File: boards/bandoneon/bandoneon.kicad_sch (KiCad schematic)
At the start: 3 parts, among them J1 Conn_01x10_Pin, J2 Conn_01x10_Pin

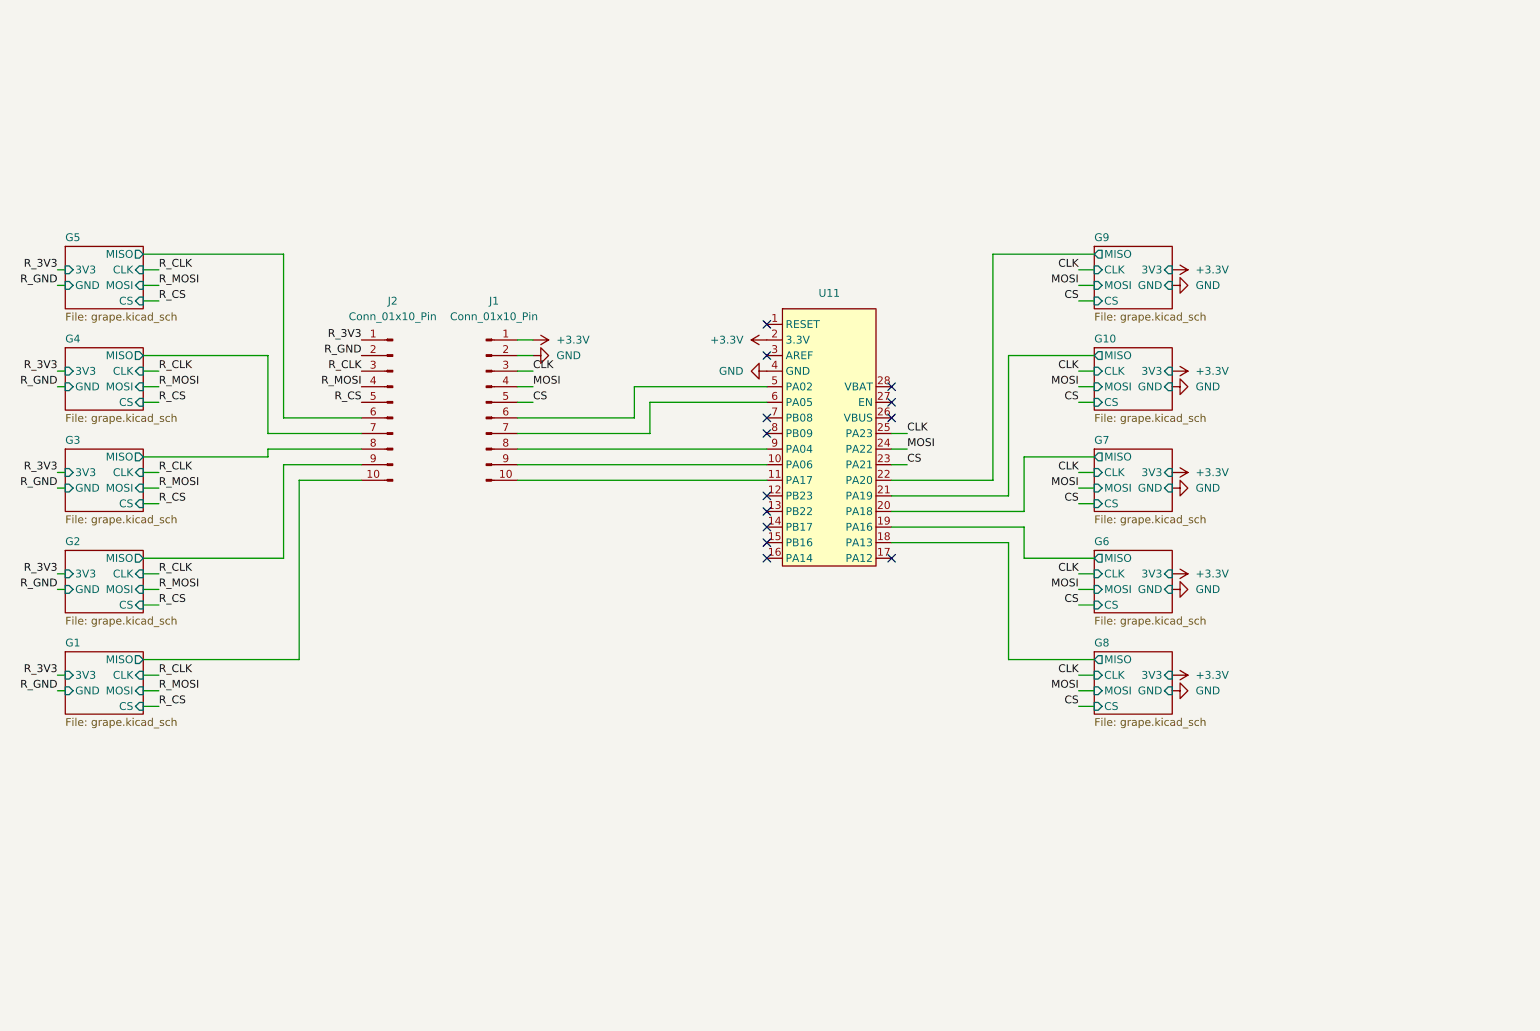
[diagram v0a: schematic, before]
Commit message: Use keyboard layout and set images DPI
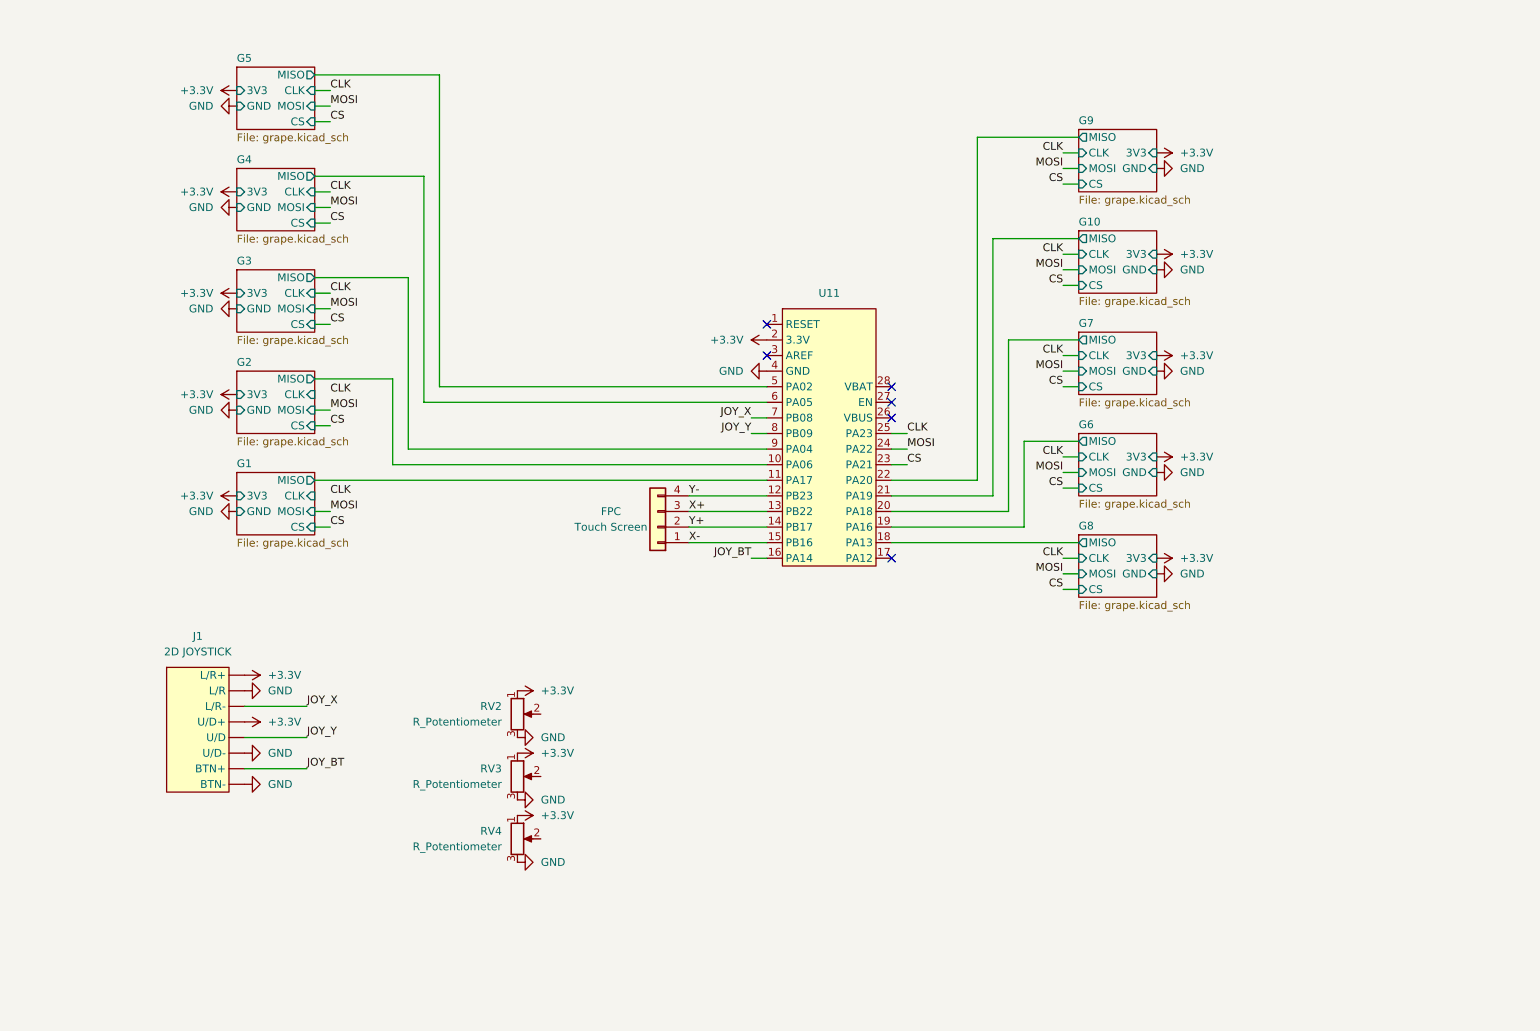
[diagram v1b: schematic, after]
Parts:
- removed J1, J2: Conn_01x10_Pin, Connector_PinHeader_1.27mm:PinHeader_1x10_P1.27mm_Vertical, symbol Connector:Conn_01x10_Pin
- added FPC: Touch Screen, Connector_FFC-FPC:TE_84952-4_1x04-1MP_P1.0mm_Horizontal, symbol Connector_Generic:Conn_01x04
- added J1: 2D JOYSTICK, symbol Library:2-Axis_Joystick
- added RV2, RV3, RV4: R_Potentiometer, symbol Device:R_Potentiometer
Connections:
- net +3.3V: now also J1. (U/D-), RV2.1, RV3.1, RV4.1
- net G1/MISO: now also U11.11 (PA17)
- net G2/MISO: now also U11.10 (PA06)
- net G3/MISO: now also U11.9 (PA04)
- net G4/MISO: now also U11.6 (PA05)
- net G5/MISO: now also U11.5 (PA02)
- net GND: now also J1. (U/D-), RV2.3, RV3.3, RV4.3
- net Y-: now reaches U11.12 (PB23)
- net Y-: now also FPC.4 (Pin_4)
- net X+: now reaches U11.13 (PB22)
- net X+: now also FPC.3 (Pin_3)
- net Y+: now reaches U11.14 (PB17)
- net Y+: now also FPC.2 (Pin_2)
- net X-: now reaches U11.15 (PB16)
- net X-: now also FPC.1 (Pin_1)
- net JOY_BT: now reaches U11.16 (PA14)
- net JOY_BT: now also J1. (U/D-)
- net JOY_X: now reaches U11.7 (PB08)
- net JOY_X: now also J1. (U/D-)
- net JOY_Y: now reaches U11.8 (PB09)
- net JOY_Y: now also J1. (U/D-)
- no-connect marks 13 -> 6

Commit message: Schamtic complete
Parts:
- removed RV3, RV4: R_Potentiometer, symbol Device:R_Potentiometer
- added J2: JST XH-3A, Connector_JST:JST_XH_B3B-XH-A_1x03_P2.50mm_Vertical, symbol Connector:Conn_01x03_Socket
- added J3: JST XH-3A, symbol Connector:Conn_01x03_Socket
- J1: footprint (none) -> Library:Adafruit (512) Analog 2-axis Thumb Joystick with Select Button
- renumbered FPC to FPC_1mm1
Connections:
- net G8/MISO is gone; now on net G1/MISO: U11.18 ((22)PA13)
- net +3.3V: now also J1.2 (X+), J1.5 (Y+), J2.3 (Pin_3); no longer J1. (U/D-), RV2.1
- net G1/MISO: no longer U11.11 (PA17)
- net G2/MISO: now also U11.16 (PA14(4)); no longer U11.10 (PA06)
- net G3/MISO: now also U11.11 (PA17(25)); no longer U11.9 (PA04)
- net G4/MISO: now also U11.10 (PA06(19/A5)); no longer U11.6 (PA05)
- net G5/MISO: now also U11.17 ((21)PA12); no longer U11.5 (PA02)
- net GND: now also J1.0 (X-), J1.3 (Y-), J1.6 (BTN-), J2.1 (Pin_1); no longer J1. (U/D-), RV2.3
- net JOY_BT: now also J1.7 (BTN+), U11.14 (PB17(0)); no longer J1. (U/D-), U11.16 (PA14)
- net JOY_X: now also J1.1 (X), U11.5 (PA02(14/A0)); no longer J1. (U/D-), U11.7 (PB08)
- net JOY_Y: now also J1.4 (Y), U11.6 (PA05(15/A1)); no longer J1. (U/D-), U11.8 (PB09)
- net at RV2.2: now also J3.2 (Pin_2)
- net X+ renamed SCR_X+
- net SCR_X+: now also U11.12 (PB23(24)); no longer U11.13 (PB22)
- net X-: no longer names the net of U11.15 (PB16(1))
- net X-: no longer FPC_1mm1.1 (Pin_1)
- net Y+ renamed SCR_Y+
- net SCR_Y+: now also U11.8 (PB09(17/A3)); no longer U11.14 (PB17)
- net Y- renamed SCR_Y-
- net SCR_Y-: now also U11.13 (PB22(23)); no longer U11.12 (PB23)
- new net: J3.3 (Pin_3), RV2.1
- new net: J3.1 (Pin_1), RV2.3
- new net POT: J2.2 (Pin_2), U11.9 (PA04(18/A4))
- new net SCR_X-: FPC_1mm1.1 (Pin_1), U11.7 (PB08(16/A2))
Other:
- removed sheet G8
- note added: "Analog reading out of Y+ and X-"
- moved on the sheet: FPC_1mm1, RV2, U11

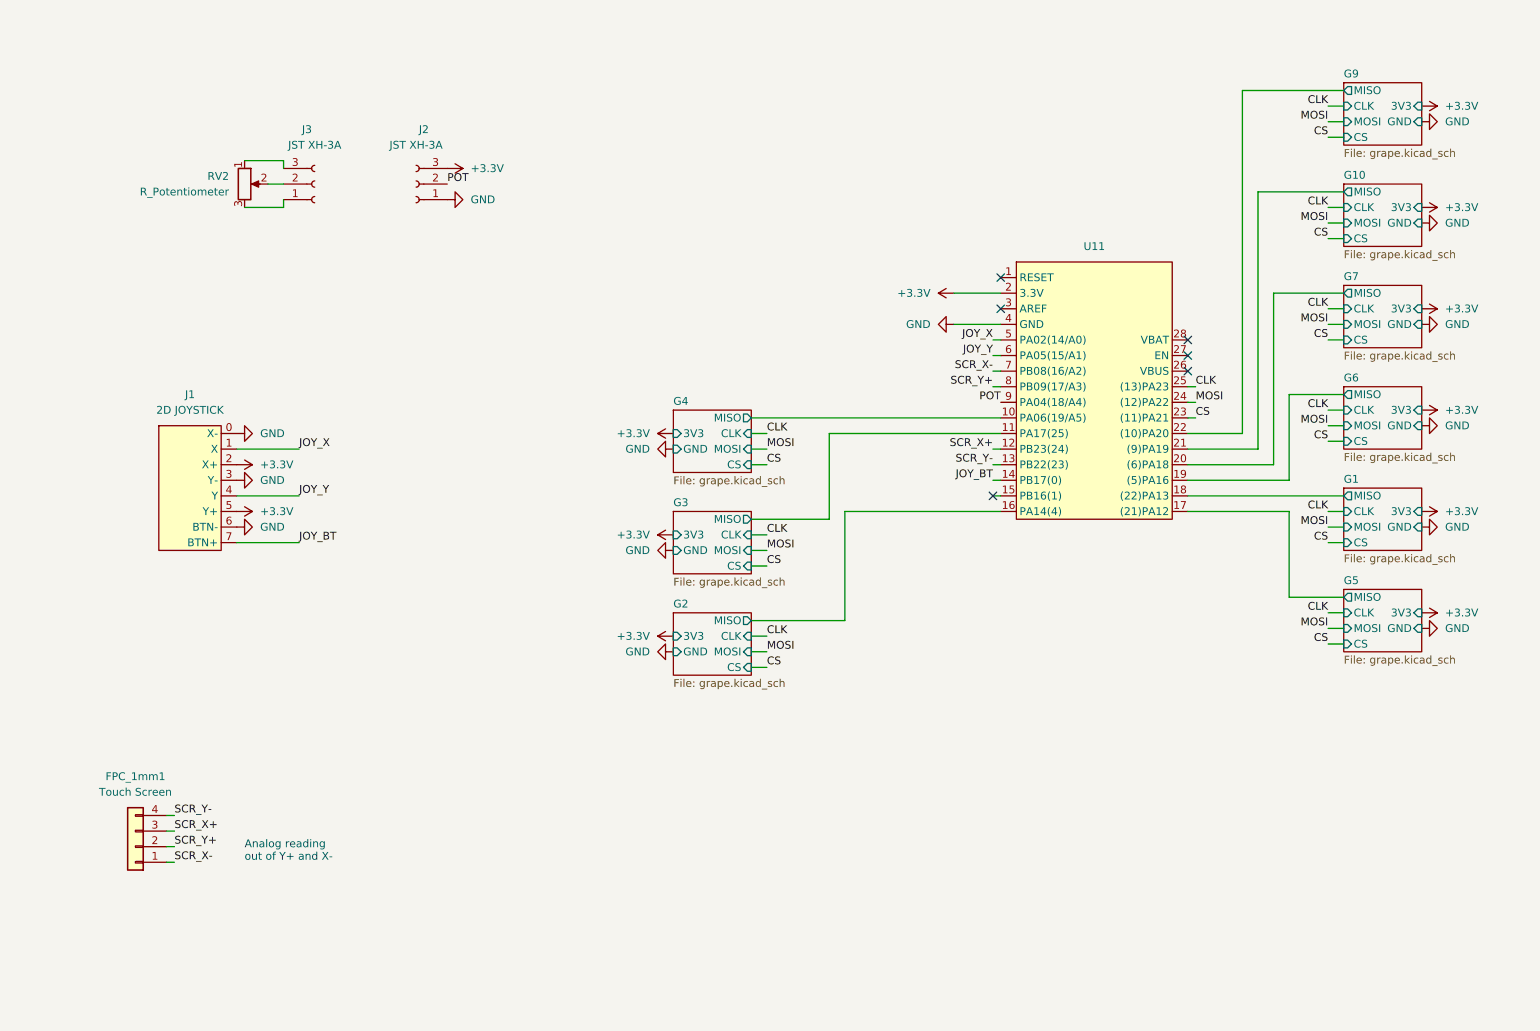
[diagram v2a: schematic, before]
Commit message: Fix component side
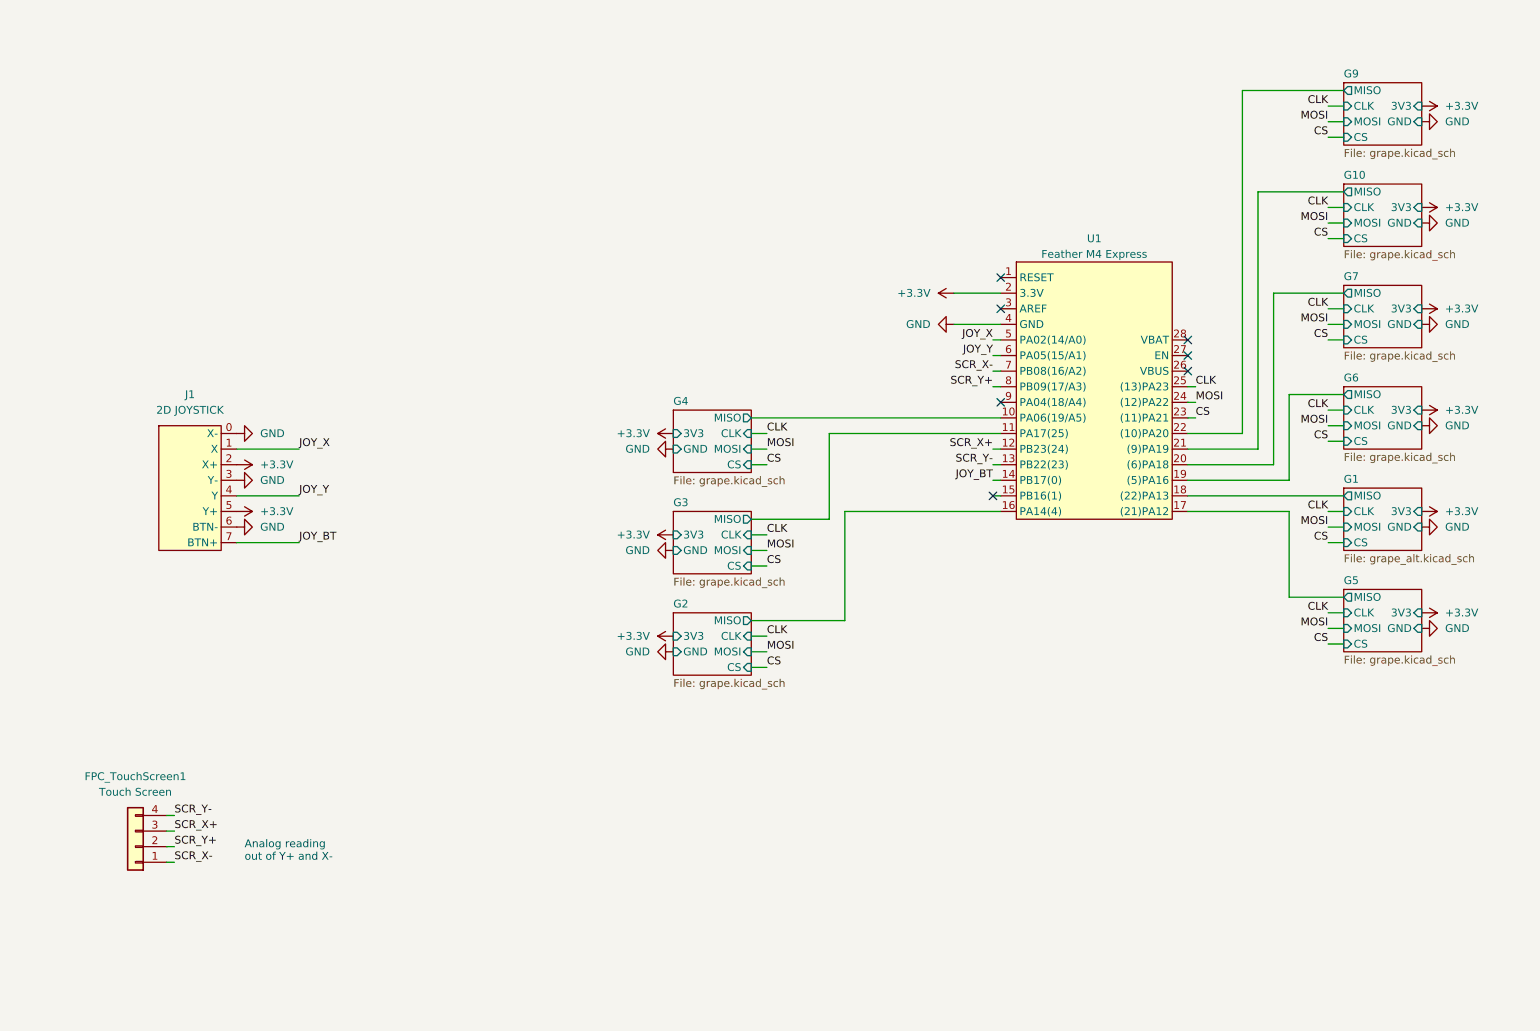
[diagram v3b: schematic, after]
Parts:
- removed J2: JST XH-3A, Connector_JST:JST_XH_B3B-XH-A_1x03_P2.50mm_Vertical, symbol Connector:Conn_01x03_Socket
- removed J3: JST XH-3A, symbol Connector:Conn_01x03_Socket
- removed RV2: R_Potentiometer, symbol Device:R_Potentiometer
- U1: renamed from U11; value ~ -> Feather M4 Express
- renumbered FPC_1mm1 to FPC_TouchScreen1
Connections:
- net POT: no longer names the net of U1.9 (PA04(18/A4))
- no-connect marks 6 -> 7
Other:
- sheet G1: file grape.kicad_sch -> grape_alt.kicad_sch

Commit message: Schema before wiring
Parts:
- removed FPC_TouchScreen1: Touch Screen, Connector_FFC-FPC:TE_84952-4_1x04-1MP_P1.0mm_Horizontal, symbol Connector_Generic:Conn_01x04
- added J4, J5: AudioJack3, Library:Jack TRS, symbol Connector_Audio:AudioJack3
- added J6, J8: JST XH-3A, symbol Connector:Conn_01x03_Socket
- added J7, J9: JST XH-3A, Connector_JST:JST_XH_B3B-XH-A_1x03_P2.50mm_Vertical, symbol Connector:Conn_01x03_Socket
- added R2: 10K, Resistor_SMD:R_0201_0603Metric, symbol Device:R
- added RV4, RV5: R_Potentiometer, symbol Device:R_Potentiometer
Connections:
- net +3.3V: now also J4.T
- net GND: now also J5.S, J7.1 (Pin_1), J9.1 (Pin_1), R2.1
- net SUS_PED: now reaches U1.15 (PB16(1))
- net SUS_PED: now also J5.T
- net P2: now reaches U1.9 (PA04(18/A4))
- net P2: now also J7.2 (Pin_2)
- net SCR_X+: no longer names the net of U1.12 (PB23(24))
- net SCR_X- renamed EXPR_PED
- net EXPR_PED: now also J4.R, R2.2
- net SCR_Y+ renamed P1
- net P1: now also J9.2 (Pin_2)
- net SCR_Y-: no longer names the net of U1.13 (PB22(23))
- new net: J8.1 (Pin_1), RV5.3
- new net: J8.2 (Pin_2), RV5.2
- new net: J8.3 (Pin_3), RV5.1
- new net: J6.3 (Pin_3), RV4.1
- new net: J6.2 (Pin_2), RV4.2
- new net: J6.1 (Pin_1), RV4.3
- new net 3V3: J7.3 (Pin_3), J9.3 (Pin_3)
- no-connect marks 7 -> 9
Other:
- note removed: "Analog reading out of Y+ and X-"
- moved on the sheet: J1, U1
